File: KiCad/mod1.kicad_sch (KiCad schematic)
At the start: 133 parts, among them J13 SFF-8654-8i, J14 RJE361882415, J17 Bus_PCI_Express_x4, J18 HDMI_A, M1 Fan_4pin, M2 Fan_4pin, Q4 2N7002, Q5 2N7002, Q6 2N7002, Q7 2N7002, U1 ZD25Q64BSIGT, U45 RTL8125BG-CG, U46 H5VU25U, U47 H5VU25U, U48 H5VU25U, U49 H5VU25U, U50 H5VU25U, U51 H5VU25U, U52 H5VU25U, U53 H5VU25U, Y7 25MHz

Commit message: Finish Connecting Module
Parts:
- removed C21: 100nF, Capacitor_SMD:C_0402_1005Metric, symbol Device:C_Small
- removed D4: LED, LED_SMD:LED_0603_1608Metric, symbol Device:LED
- removed U1: ZD25Q64BSIGT, Package_SO:SOIC-8_5.3x5.3mm_P1.27mm, symbol Memory_Flash:W25Q128JVS
- added C15, C16, C17, C18: 220nF, Capacitor_SMD:C_0402_1005Metric, symbol Device:C_Small
- added R26: 4.7k, Resistor_SMD:R_0402_1005Metric, symbol Device:R_Small
- R12: value 10k -> 4.7k
- R14: value 2.2k -> 4.7k
- R21: value 10k -> 1k
- R22: value 10k -> 15k
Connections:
- net ETH.REFCLK+ is gone; now on net NVME0_REFCLK+: A1.85 (REFCLK0+)
- net ETH.REFCLK- is gone; now on net NVME0_REFCLK-: A1.87 (REFCLK0-)
- net ETH.SMBCLK is gone; now on net SMB_DATA: A1.106 (SMB_CLK)
- net ETH.SMBDAT is gone; now on net SMB_CLK: A1.108 (SMB_DATA)
- net ETH.~{PLTRST} is gone; now on net ~{PCIE_RST}: A1.105 (~{PLTRST})
- net ETH.~{WAKE} is gone; now on net ~{PCIE_WAKE}: A1.103 (~{WAKE})
- net NVME.REFCLK+ is gone; now on net NVME1_REFCLK+: A1.91 (REFCLK1+)
- net NVME.REFCLK- is gone; now on net NVME1_REFCLK-: A1.93 (REFCLK1-)
- net +3V3: now also R14.1, R24.2; no longer R14.2, R22.1, R223.1
- net +3V3SB: now also R12.2, R223.1, R26.2
- net ETH_LED1: now also R26.1
- net ETH_REFCLK+: now also A1.88 (REFCLK3+)
- net ETH_REFCLK-: now also A1.90 (REFCLK3-)
- net GND: now also R22.2; no longer R12.2, R24.2
- net NVME0_RX+: now also A1.28 (HSIO2_RX+)
- net NVME0_RX-: now also A1.30 (HSIO2_RX-)
- net NVME0_TX+: now also C15.1
- net NVME0_TX-: now also C16.1
- net NVME1_RX+: now also A1.34 (HSIO3_RX+)
- net NVME1_RX-: now also A1.36 (HSIO3_RX-)
- net NVME1_TX+: now also C17.1
- net NVME1_TX-: now also C18.1
- net PCIEX4_REFCLK+: now also A1.97 (REFCLK2+)
- net PCIEX4_REFCLK-: now also A1.99 (REFCLK2-)
- net POWER_S0: now also R21.2, R22.1
- net at A1.161 (SPI_IO2): no longer R22.2
- net at A1.153 (SPI_IO3): no longer R21.2
- net at U45.3 (GPI): now also R12.1
- net ~{ETH_CLKREQ}: now reaches U45.48 (CLKREQB)
- net ~{ETH_CLKREQ}: now also A1.100 (~{CLKREQ3}), R14.2
- net at A1.25 (HSIO2_TX+): now also C15.2
- net at A1.27 (HSIO2_TX-): now also C16.2
- net at A1.31 (HSIO3_TX+): now also C17.2
- net at A1.33 (HSIO3_TX-): now also C18.2
- net HDD_LED: no longer names the net of A1.123 (GPP_B14)
- net NVME.SUSCLK: no longer names the net of A1.131 (SUSCLK)
- net PGM_INT: no longer names the net of A1.132 (GPP_D2)
- net PGM_SCL: no longer names the net of A1.154 (I2C2_SCL)
- net PGM_SDA: no longer names the net of A1.156 (I2C2_SDA)
- net TYPE_C_HEADER.D+: no longer names the net of A1.112 (USB2_P6+)
- net TYPE_C_HEADER.D-: no longer names the net of A1.114 (USB2_P6-)
- net TYPE_C_SCL: no longer names the net of A1.147 (SML1_CLK)
- net TYPE_C_SDA: no longer names the net of A1.145 (SML1_DATA)
- net ~{TYPE_C_PMCALERT}: no longer names the net of A1.125 (GPP_B11)
- no-connect marks 128 -> 142
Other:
- moved on the sheet: R223, R24

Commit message: add pretty sections
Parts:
- removed R10, R11: 100R, Resistor_SMD:R_0402_1005Metric, symbol Device:R_Small
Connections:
- net SLOT4_UART_RX is gone; now on net SLOT2_UART_RX: R17.2
- net SLOT4_UART_TX is gone; now on net SLOT2_UART_TX: R18.2
- net SLOT5_UART_RX is gone; now on net SLOT3_UART_RX: R19.2
- net SLOT5_UART_TX is gone; now on net SLOT3_UART_TX: R20.2
- net SLOT3_UART_RX: no longer R15.2
- net SLOT3_UART_TX: no longer R16.2
- new net BMC_UART_RX: R15.2
- new net BMC_UART_TX: R16.2
- no-connect marks 142 -> 144
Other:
- note added: "2.5G Ethernet"
- note added: "2x U.2 NVME"
- note added: "Fans"
- note added: "HDMI"
- note added: "LattePanda Mu Module"
- note added: "PCIe x4 Slot"
- note added: "Power LED"
- note added: "USB 3"
- moved on the sheet: A1, C1, C10, C11, C12, C13, C14, C15, C16, C163, C164, C165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

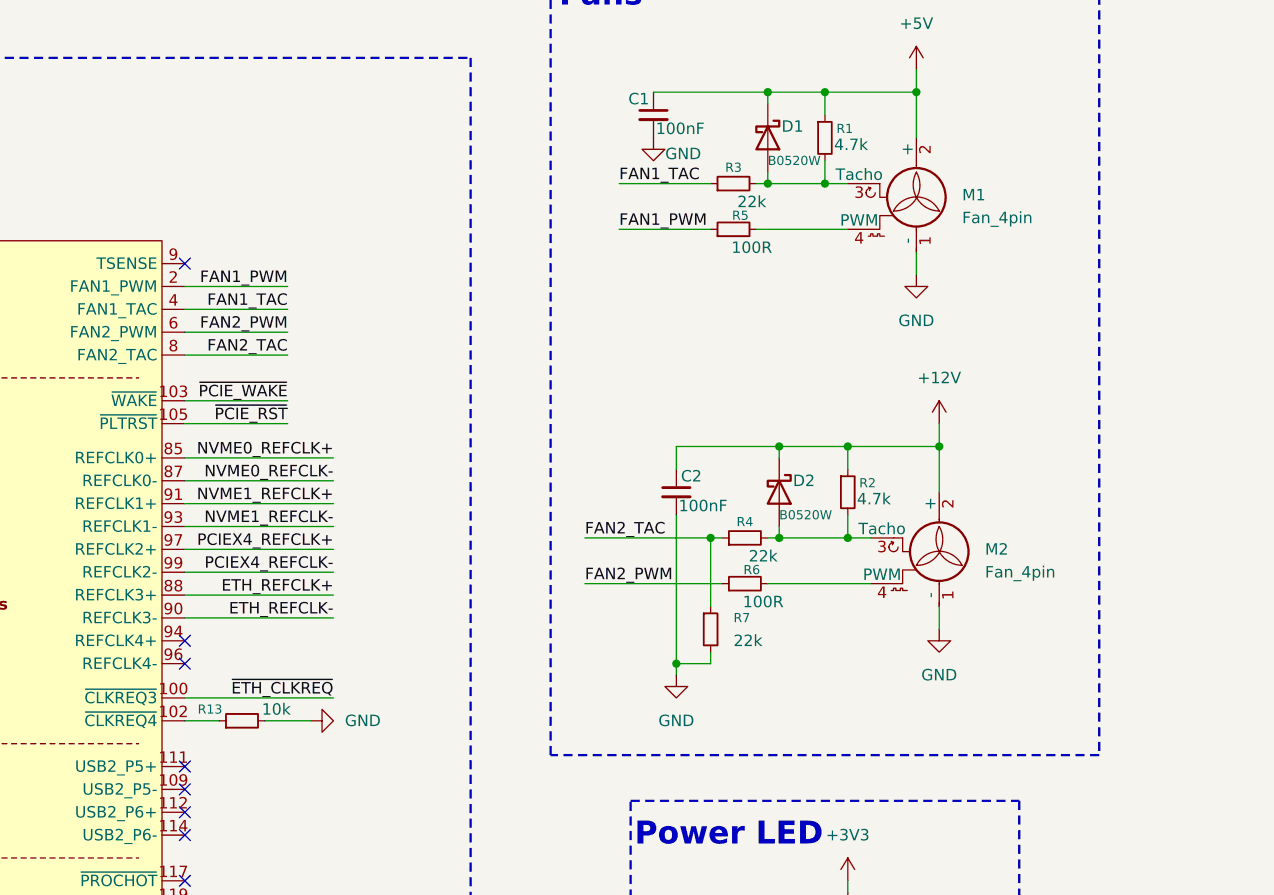
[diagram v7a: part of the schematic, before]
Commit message: Copy modules 2 and 3, remove unnecessary pages
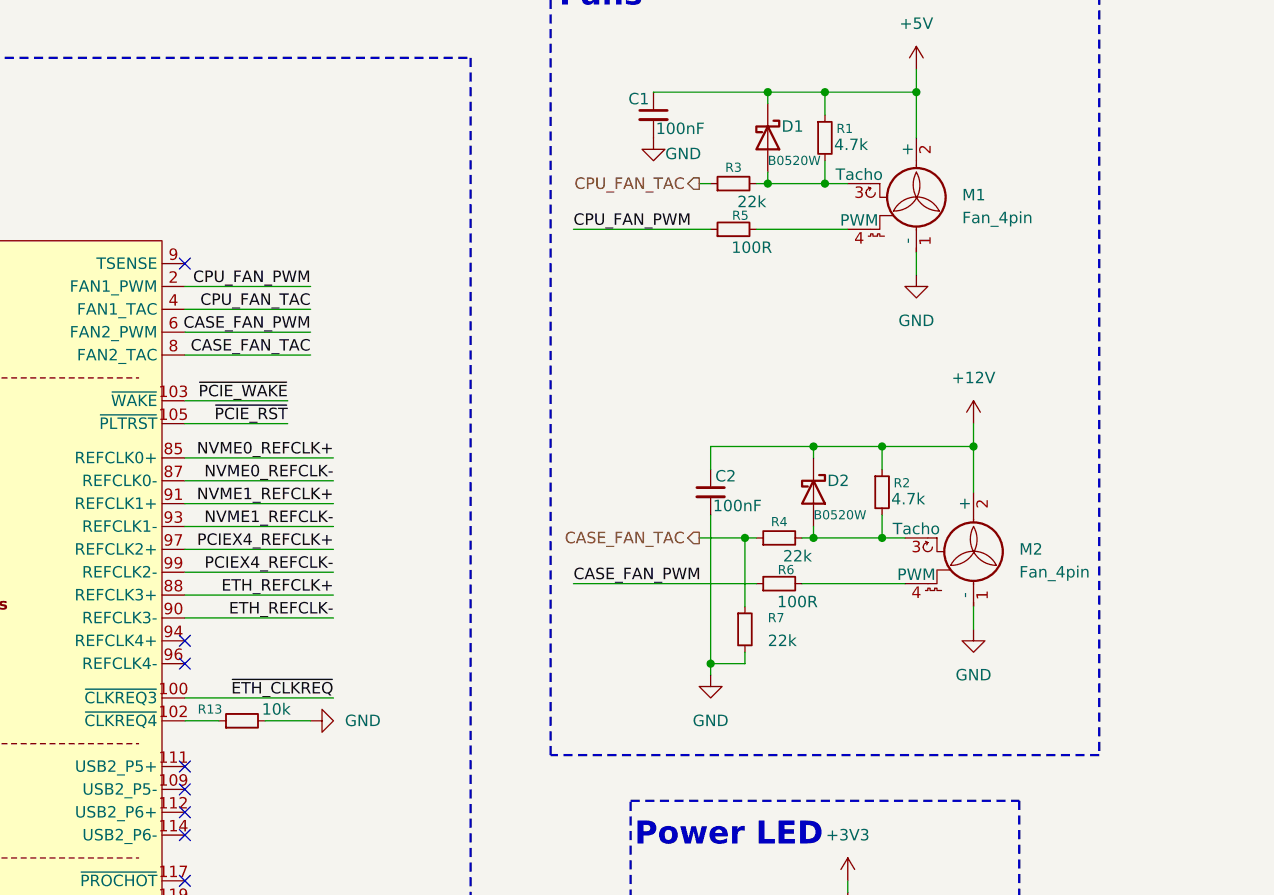
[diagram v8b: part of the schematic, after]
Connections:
- net FAN1_PWM renamed CPU_FAN_PWM
- net FAN1_TAC renamed CPU_FAN_TAC
- net FAN2_PWM renamed CASE_FAN_PWM
- net FAN2_TAC renamed CASE_FAN_TAC
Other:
- moved on the sheet: C2, D2, M2, R2, R4, R6, R7
